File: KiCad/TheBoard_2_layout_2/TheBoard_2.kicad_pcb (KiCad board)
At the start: 2 copper layers, 150 x 100 mm, 163 parts, among them J1 Conn_01x03_Female, J2 Conn_01x03_Female, J3 Conn_01x16_Female, J5 Conn_01x16_Female, J6 Conn_01x02_Male, J7 Conn_02x18_Counter_Clockwise, U1 MAX680CSA+T, U10 MCP6074-E/SL, U11 MCP6074-E/SL, U12 MCP6074-E/SL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

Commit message: board2-layout2 complete
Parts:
- removed J7: Conn_02x18_Counter_Clockwise, Connector_PinHeader_2.54mm:PinHeader_2x18_P2.54mm_Vertical
- added J4: DB37_Male_MountingHoles, Connector_Dsub:DSUB-37_Male_Horizontal_P2.77x2.84mm_EdgePinOffset7.70mm_Housed_MountingHolesOffset9.12mm, B.Cu at (156.5, 122.9)
- moved C1 36.8 mm to (148.4, 56.3), turned to -90 degrees
- moved C2 35.0 mm to (134.6, 62.8), turned to 0 degrees
- moved U1 34.1 mm to (133.2, 57.7), turned to 90 degrees
- moved C5 30.9 mm to (165.8, 51.4), turned to 0 degrees
- moved RV1 28.4 mm to (184.2, 56.9), turned to -90 degrees
- moved U2 27.2 mm to (178.2, 55.9), turned to 180 degrees
- moved C4 21.4 mm to (165.9, 57.9), turned to 0 degrees
- moved R2 20.3 mm to (179.2, 51.1), turned to 180 degrees
- moved C3 18.9 mm to (148.2, 50.5)
- moved J6 16.8 mm to (157.7, 51.1)
- moved U6 2.67 mm to (165.8, 114.0)
- moved U7 2.67 mm to (165.8, 103.5)
- moved U8 2.67 mm to (165.8, 93.2)
- moved U9 2.67 mm to (166.1, 83.0)
- moved R100 2.21 mm to (175.6, 123.9)
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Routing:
- net +5V: track 0.00 -> 448.4 mm
- net +2V5: track 26.8 -> 373.8 mm
- net -5V: track 11.0 -> 341.8 mm
- net Net-(J5-Pad13): track 4.80 -> 32.5 mm
- net Net-(J3-Pad4): track 4.39 -> 27.7 mm
- net Net-(J5-Pad4): track 4.39 -> 27.3 mm
- net Net-(J3-Pad13): track 4.40 -> 27.2 mm
- net Net-(J3-Pad3): track 7.22 -> 29.8 mm
- net Net-(R18-Pad2): track 14.5 -> 36.9 mm
- net Net-(R33-Pad2): track 14.3 -> 36.5 mm
- net Net-(R19-Pad2): track 2.57 -> 24.7 mm
- net Net-(J5-Pad3): track 7.20 -> 29.3 mm
- net Net-(J3-Pad14): track 7.20 -> 29.3 mm
- net Net-(J5-Pad14): track 8.00 -> 29.9 mm
- net Net-(R32-Pad2): track 2.51 -> 24.3 mm
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
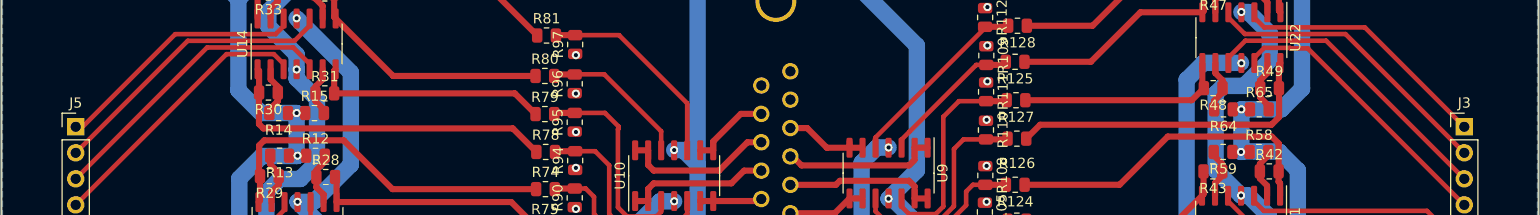
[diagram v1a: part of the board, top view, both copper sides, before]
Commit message: Change pin header to female
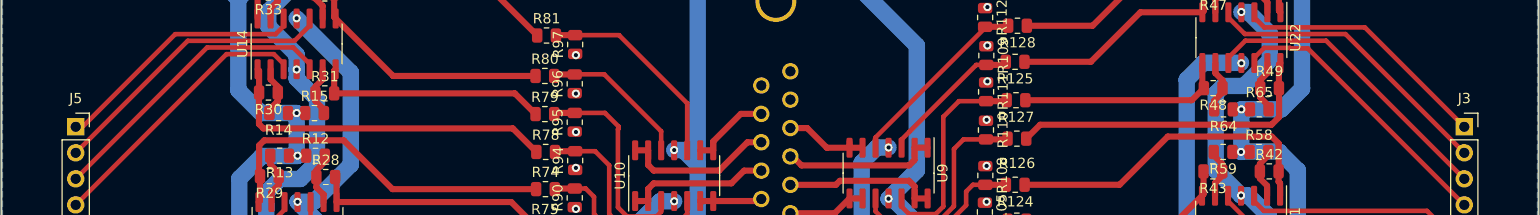
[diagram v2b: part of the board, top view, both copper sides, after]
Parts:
- J3, J5: footprint Connector_PinHeader_2.54mm:PinHeader_1x16_P2.54mm_Vertical -> Connector_PinSocket_2.54mm:PinSocket_1x16_P2.54mm_Vertical
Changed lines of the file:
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@@
     )
   )
-  (footprint "Connector_PinHeader_2.54mm:PinHeader_1x16_P2.54mm_Vertical" locked (layer "F.Cu")
+  (footprint "Connector_PinSocket_2.54mm:PinSocket_1x16_P2.54mm_Vertical" locked (layer "F.Cu")
     (at 86.75 78.45)
-    (descr "Through hole straight pin header, 1x16, 2.54mm pitch, single row")
-    (tags "Through hole pin header THT 1x16 2.54mm single row")
+    (descr "Through hole straight socket strip, 1x16, 2.54mm pitch, single row (from Kicad 4.0.7), script generated")
+    (tags "Through hole socket strip THT 1x16 2.54mm single row")
     (property "Sheetfile" "TheBoard_2.kicad_sch")
     (property "Sheetname" "")
     (attr through_hole)
-    (fp_text reference "J5" (at 0 -2.33) (layer "F.SilkS")
-      (effects (font (size 1 1) (thickness 0.15)))
-    )
-    (fp_text value "Conn_01x16_Female" (at 0 40.43) (layer "F.Fab")
+    (fp_text reference "J5" (at 0 -2.77) (layer "F.SilkS")
+      (effects (font (size 1 1) (thickness 0.15)))
+    )
+    (fp_text value "Conn_01x16_Female" (at 0 40.87) (layer "F.Fab")
       (effects (font (size 1 1) (thickness 0.15)))
     )
@@
     )
     (fp_line (start -1.33 39.43) (end 1.33 39.43) (layer "F.SilkS") (width 0.12))
-    (fp_line (start -1.33 1.27) (end -1.33 39.43) (layer "F.SilkS") (width 0.12))
+    (fp_line (start 0 -1.33) (end 1.33 -1.33) (layer "F.SilkS") (width 0.12))
     (fp_line (start 1.33 1.27) (end 1.33 39.43) (layer "F.SilkS") (width 0.12))
     (fp_line (start -1.33 1.27) (end 1.33 1.27) (layer "F.SilkS") (width 0.12))
-    (fp_line (start -1.33 -1.33) (end 0 -1.33) (layer "F.SilkS") (width 0.12))
-    (fp_line (start -1.33 0) (end -1.33 -1.33) (layer "F.SilkS") (width 0.12))
-    (fp_line (start 1.8 39.9) (end 1.8 -1.8) (layer "F.CrtYd") (width 0.05))
-    (fp_line (start -1.8 39.9) (end 1.8 39.9) (layer "F.CrtYd") (width 0.05))
-    (fp_line (start 1.8 -1.8) (end -1.8 -1.8) (layer "F.CrtYd") (width 0.05))
-    (fp_line (start -1.8 -1.8) (end -1.8 39.9) (layer "F.CrtYd") (width 0.05))
+    (fp_line (start -1.33 1.27) (end -1.33 39.43) (layer "F.SilkS") (width 0.12))
+    (fp_line (start 1.33 -1.33) (end 1.33 0) (layer "F.SilkS") (width 0.12))
+    (fp_line (start -1.8 39.9) (end -1.8 -1.8) (layer "F.CrtYd") (width 0.05))
+    (fp_line (start -1.8 -1.8) (end 1.75 -1.8) (layer "F.CrtYd") (width 0.05))
+    (fp_line (start 1.75 39.9) (end -1.8 39.9) (layer "F.CrtYd") (width 0.05))
+    (fp_line (start 1.75 -1.8) (end 1.75 39.9) (layer "F.CrtYd") (width 0.05))
+    (fp_line (start -1.27 -1.27) (end 0.635 -1.27) (layer "F.Fab") (width 0.1))
+    (fp_line (start 1.27 -0.635) (end 1.27 39.37) (layer "F.Fab") (width 0.1))
+    (fp_line (start 0.635 -1.27) (end 1.27 -0.635) (layer "F.Fab") (width 0.1))
+    (fp_line (start -1.27 39.37) (end -1.27 -1.27) (layer "F.Fab") (width 0.1))
     (fp_line (start 1.27 39.37) (end -1.27 39.37) (layer "F.Fab") (width 0.1))
-    (fp_line (start -1.27 39.37) (end -1.27 -0.635) (layer "F.Fab") (width 0.1))
-    (fp_line (start -0.635 -1.27) (end 1.27 -1.27) (layer "F.Fab") (width 0.1))
-    (fp_line (start 1.27 -1.27) (end 1.27 39.37) (layer "F.Fab") (width 0.1))
-    (fp_line (start -1.27 -0.635) (end -0.635 -1.27) (layer "F.Fab") (width 0.1))
     (pad "1" thru_hole rect locked (at 0 0) (size 1.7 1.7) (drill 1) (layers *.Cu *.Mask)
       (net 20 "Net-(J5-Pad1)") (pinfunction "Pin_1") (pintype "passive"))
@@
     (pad "16" thru_hole oval locked (at 0 38.1) (size 1.7 1.7) (drill 1) (layers *.Cu *.Mask)
       (net 35 "Net-(J5-Pad16)") (pinfunction "Pin_16") (pintype "passive"))
-    (model "${KICAD6_3DMODEL_DIR}/Connector_PinHeader_2.54mm.3dshapes/PinHeader_1x16_P2.54mm_Vertical.wrl"
+    (model "${KICAD6_3DMODEL_DIR}/Connector_PinSocket_2.54mm.3dshapes/PinSocket_1x16_P2.54mm_Vertical.wrl"
       (offset (xyz 0 0 0))
       (scale (xyz 1 1 1))
@@
     )
   )
-  (footprint "Connector_PinHeader_2.54mm:PinHeader_1x16_P2.54mm_Vertical" locked (layer "F.Cu")
+  (footprint "Connector_PinSocket_2.54mm:PinSocket_1x16_P2.54mm_Vertical" locked (layer "F.Cu")
     (at 222.25 78.45)
-    (descr "Through hole straight pin header, 1x16, 2.54mm pitch, single row")
-    (tags "Through hole pin header THT 1x16 2.54mm single row")
+    (descr "Through hole straight socket strip, 1x16, 2.54mm pitch, single row (from Kicad 4.0.7), script generated")
+    (tags "Through hole socket strip THT 1x16 2.54mm single row")
     (property "Sheetfile" "TheBoard_2.kicad_sch")
     (property "Sheetname" "")
     (attr through_hole)
-    (fp_text reference "J3" (at 0 -2.33) (layer "F.SilkS")
-      (effects (font (size 1 1) (thickness 0.15)))
-    )
-    (fp_text value "Conn_01x16_Female" (at 0 40.43) (layer "F.Fab")
+    (fp_text reference "J3" (at 0 -2.77) (layer "F.SilkS")
+      (effects (font (size 1 1) (thickness 0.15)))
+    )
+    (fp_text value "Conn_01x16_Female" (at 0 40.87) (layer "F.Fab")
       (effects (font (size 1 1) (thickness 0.15)))
     )
@@
     )
     (fp_line (start 1.33 1.27) (end 1.33 39.43) (layer "F.SilkS") (width 0.12))
-    (fp_line (start -1.33 39.43) (end 1.33 39.43) (layer "F.SilkS") (width 0.12))
+    (fp_line (start 1.33 -1.33) (end 1.33 0) (layer "F.SilkS") (width 0.12))
     (fp_line (start -1.33 1.27) (end 1.33 1.27) (layer "F.SilkS") (width 0.12))
     (fp_line (start -1.33 1.27) (end -1.33 39.43) (layer "F.SilkS") (width 0.12))
-    (fp_line (start -1.33 0) (end -1.33 -1.33) (layer "F.SilkS") (width 0.12))
-    (fp_line (start -1.33 -1.33) (end 0 -1.33) (layer "F.SilkS") (width 0.12))
-    (fp_line (start -1.8 39.9) (end 1.8 39.9) (layer "F.CrtYd") (width 0.05))
-    (fp_line (start 1.8 39.9) (end 1.8 -1.8) (layer "F.CrtYd") (width 0.05))
-    (fp_line (start -1.8 -1.8) (end -1.8 39.9) (layer "F.CrtYd") (width 0.05))
-    (fp_line (start 1.8 -1.8) (end -1.8 -1.8) (layer "F.CrtYd") (width 0.05))
+    (fp_line (start -1.33 39.43) (end 1.33 39.43) (layer "F.SilkS") (width 0.12))
+    (fp_line (start 0 -1.33) (end 1.33 -1.33) (layer "F.SilkS") (width 0.12))
+    (fp_line (start 1.75 -1.8) (end 1.75 39.9) (layer "F.CrtYd") (width 0.05))
+    (fp_line (start -1.8 39.9) (end -1.8 -1.8) (layer "F.CrtYd") (width 0.05))
+    (fp_line (start -1.8 -1.8) (end 1.75 -1.8) (layer "F.CrtYd") (width 0.05))
+    (fp_line (start 1.75 39.9) (end -1.8 39.9) (layer "F.CrtYd") (width 0.05))
+    (fp_line (start 1.27 -0.635) (end 1.27 39.37) (layer "F.Fab") (width 0.1))
+    (fp_line (start -1.27 39.37) (end -1.27 -1.27) (layer "F.Fab") (width 0.1))
+    (fp_line (start -1.27 -1.27) (end 0.635 -1.27) (layer "F.Fab") (width 0.1))
     (fp_line (start 1.27 39.37) (end -1.27 39.37) (layer "F.Fab") (width 0.1))
-    (fp_line (start -1.27 -0.635) (end -0.635 -1.27) (layer "F.Fab") (width 0.1))
-    (fp_line (start 1.27 -1.27) (end 1.27 39.37) (layer "F.Fab") (width 0.1))
-    (fp_line (start -0.635 -1.27) (end 1.27 -1.27) (layer "F.Fab") (width 0.1))
-    (fp_line (start -1.27 39.37) (end -1.27 -0.635) (layer "F.Fab") (width 0.1))
+    (fp_line (start 0.635 -1.27) (end 1.27 -0.635) (layer "F.Fab") (width 0.1))
     (pad "1" thru_hole rect locked (at 0 0) (size 1.7 1.7) (drill 1) (layers *.Cu *.Mask)
       (net 4 "Net-(J3-Pad1)") (pinfunction "Pin_1") (pintype "passive"))
@@
     (pad "16" thru_hole oval locked (at 0 38.1) (size 1.7 1.7) (drill 1) (layers *.Cu *.Mask)
       (net 106 "Net-(J3-Pad16)") (pinfunction "Pin_16") (pintype "passive"))
-    (model "${KICAD6_3DMODEL_DIR}/Connector_PinHeader_2.54mm.3dshapes/PinHeader_1x16_P2.54mm_Vertical.wrl"
-      (offset (xyz 0 0 0))
-      (scale (xyz 1 1 1))
+    (model "${KICAD6_3DMODEL_DIR}/Connector_PinSocket_2.54mm.3dshapes/PinSocket_1x16_P2.54mm_Vertical.wrl"
+      (offset (xyz 0 0 0))
+      (scale (xyz 1 1 1))

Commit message: Adding jumpers, checking GND
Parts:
- added J7: Conn_01x02_Pin, Connector_PinHeader_2.54mm:PinHeader_1x02_P2.54mm_Vertical, F.Cu at (160.5, 57.0)
- added J8: Conn_01x02_Male, Connector_PinHeader_2.54mm:PinHeader_1x02_P2.54mm_Vertical, F.Cu at (127.0, 53.0)
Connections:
- C5 pad 2: -5V -> Net-(J7-Pin_1)
- R2 pad 2: -5V -> Net-(J7-Pin_1)
- U1 pad 6: +5V -> Net-(J8-Pin_1)
- U2 pad 3: -5V -> Net-(J7-Pin_1)
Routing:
- net +2V5: track 373.8 -> 265.3 mm
- net +5V: track 448.4 -> 394.5 mm
- net Net-(J7-Pin_1): track 0.00 -> 21.2 mm
- net -5V: track 341.8 -> 362.0 mm
- net Net-(J8-Pin_1): track 0.00 -> 13.0 mm
- net Net-(U13-VINB+): track 18.6 -> 17.9 mm

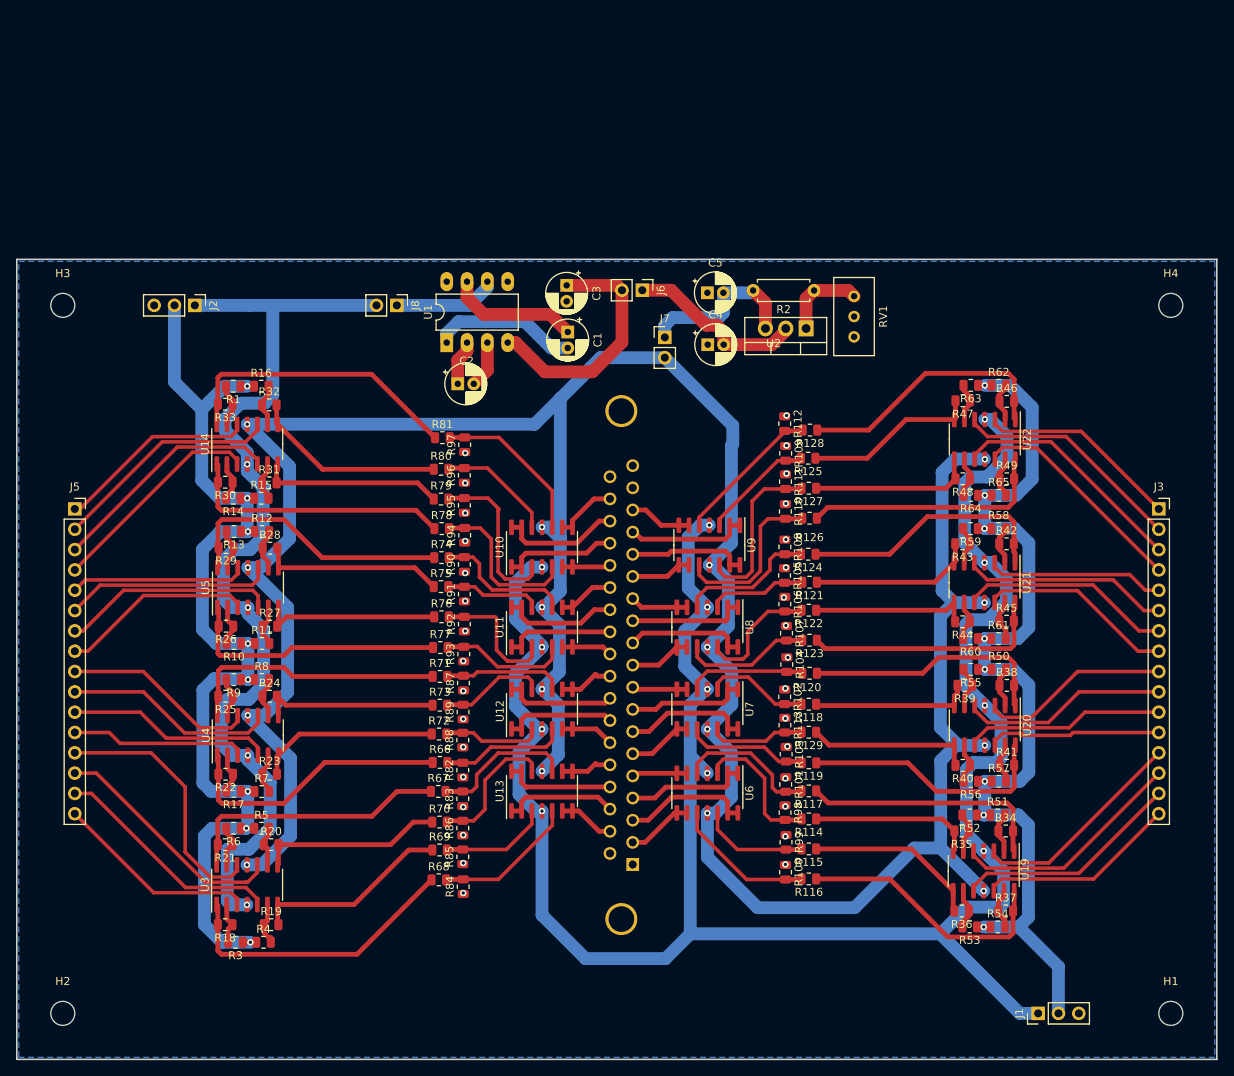
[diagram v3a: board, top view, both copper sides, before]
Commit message: re-routing power
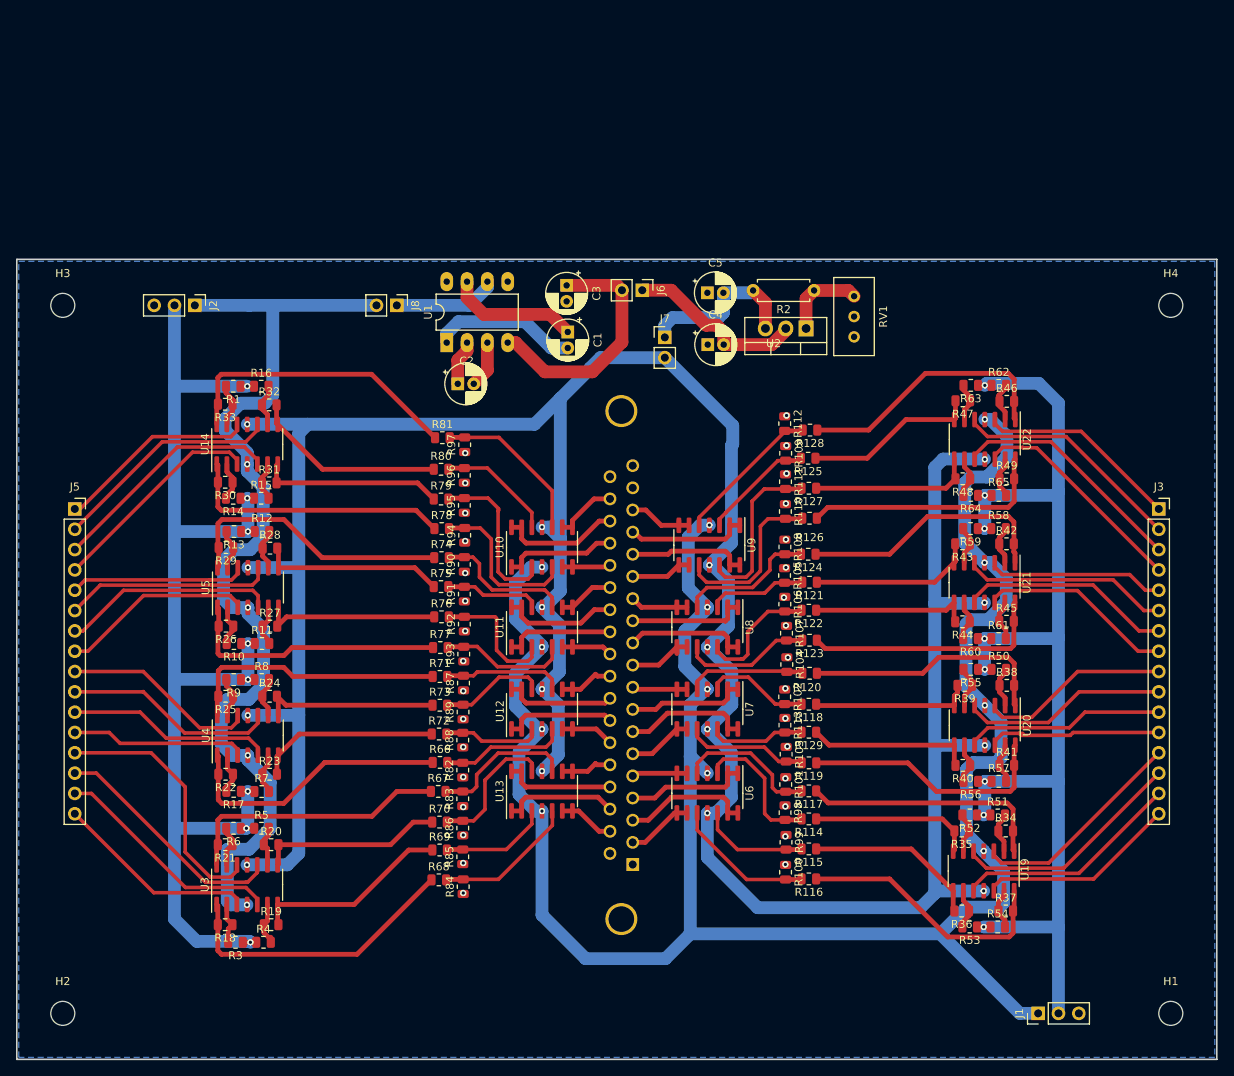
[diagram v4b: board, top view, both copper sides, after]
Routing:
- net +2V5: track 265.3 -> 300.7 mm
- net -5V: track 362.0 -> 369.3 mm

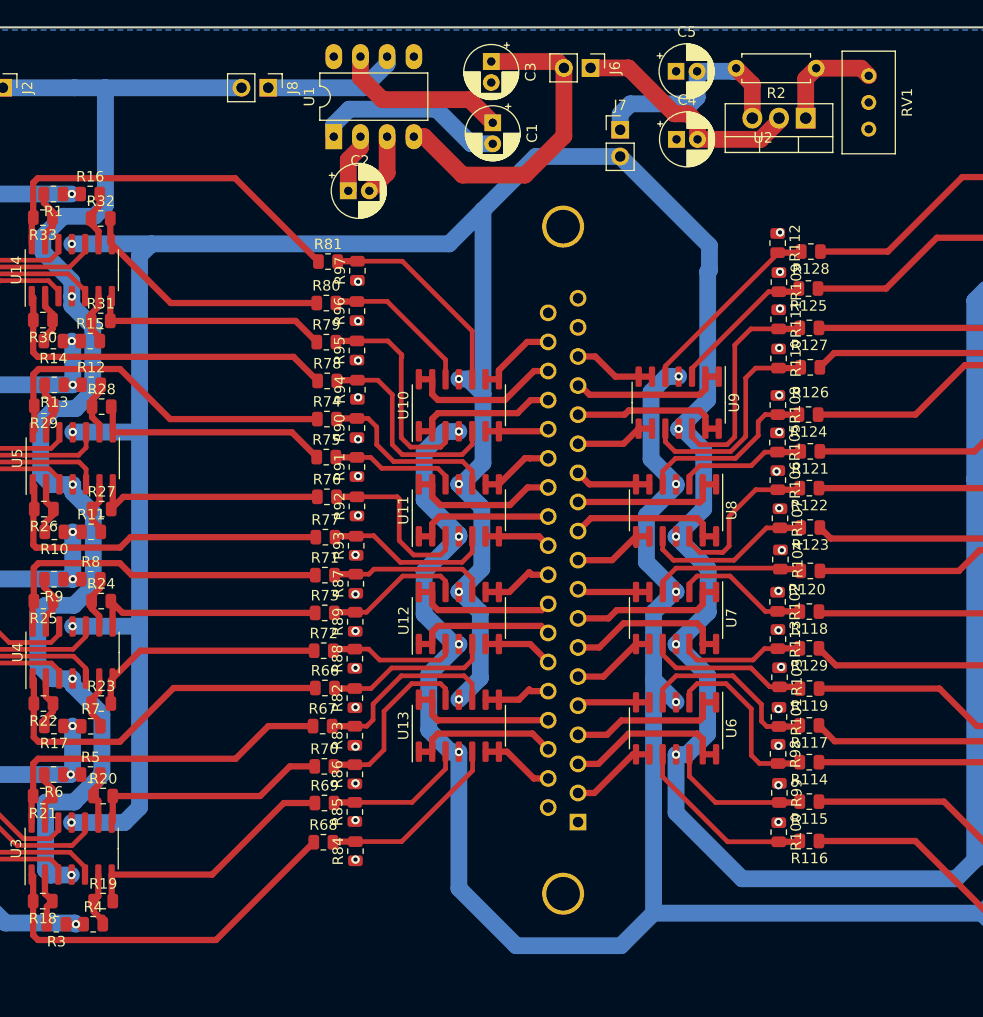
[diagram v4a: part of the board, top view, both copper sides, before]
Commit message: Re-routing power
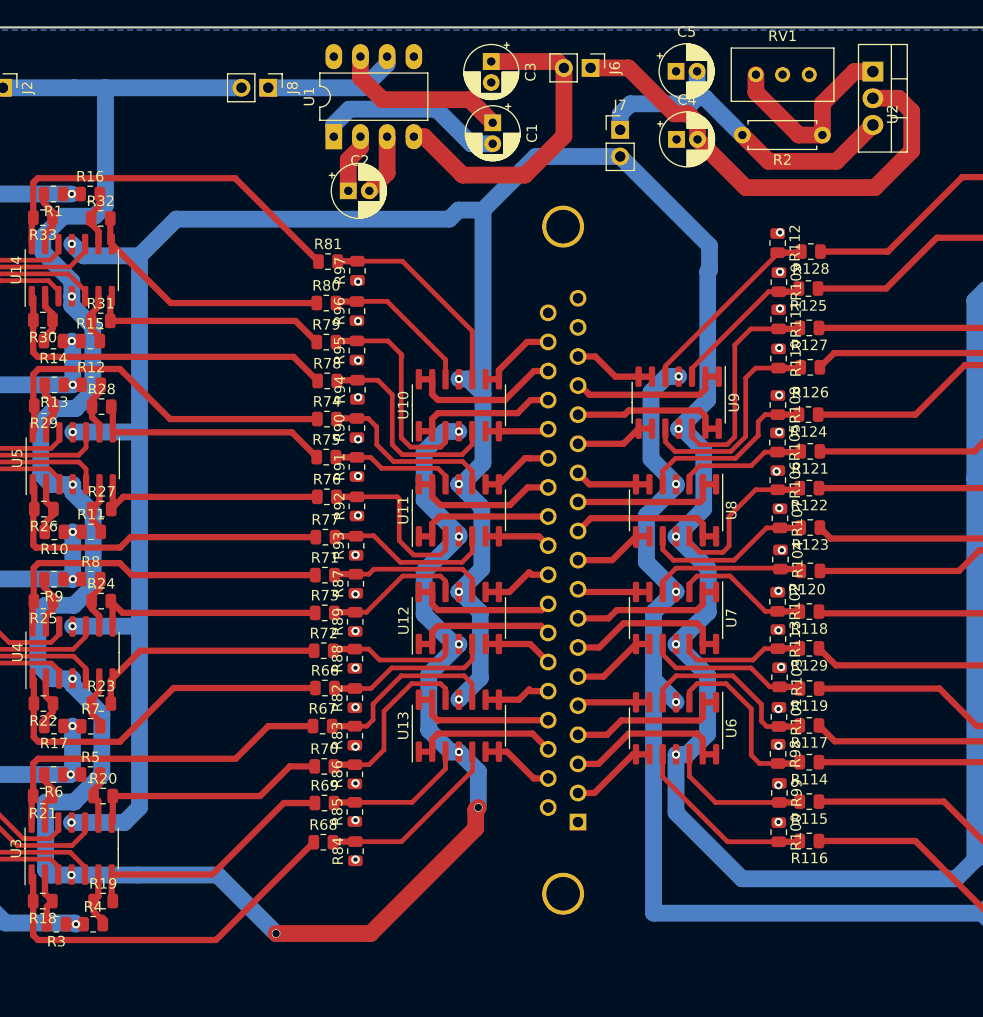
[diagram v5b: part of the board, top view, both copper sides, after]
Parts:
- moved U2 7.78 mm to (184.6, 51.5), turned to -90 degrees
- moved RV1 7.68 mm to (178.5, 51.8), turned to 0 degrees
- moved R2 6.39 mm to (179.8, 57.5)
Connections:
- J4 pad 0: unconnected-(J4-PAD-Pad0) -> GND
- J4 pad 1: unconnected-(J4-Pad1) -> GND
- J4 pad 19: unconnected-(J4-Pad19) -> GND
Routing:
- net Net-(J6-Pin_1): track 22.7 -> 45.6 mm
- net +5V: track 394.5 -> 412.5 mm, vias 16 -> 18
- net Net-(J7-Pin_1): track 21.2 -> 32.7 mm
- net Net-(U2-ADJ): track 10.5 -> 18.8 mm
- net -5V: track 369.3 -> 368.6 mm
